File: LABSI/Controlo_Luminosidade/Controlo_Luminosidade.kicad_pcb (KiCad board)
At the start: 2 copper layers, 60 x 80 mm, 41 parts, among them J1 5V/4A, J10 Touch Button, J11 Touch Button, J12 Touch Button, J2 Barrel_Jack_Switch, J3 Conn_01x05_Pin, J4 Conn_01x04_Pin, J5 Conn_01x04_Pin, J6 AVR-ISP-6, J7 Conn_01x03_Pin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

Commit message: pcb finalizado, gee«rbers gerados, falta desenvolver o que falta no ultimo commit
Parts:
- removed C9: 0.1u, Capacitor_THT:C_Disc_D3.0mm_W2.0mm_P2.50mm
- added J13: ESP32, Connector_PinSocket_2.54mm:PinSocket_1x04_P2.54mm_Vertical, F.Cu at (135.8, 68.2)
- added R8: 6.8k, Resistor_THT:R_Axial_DIN0204_L3.6mm_D1.6mm_P5.08mm_Horizontal, F.Cu at (145.3, 71.3)
- added R9: 10k, Resistor_THT:R_Axial_DIN0204_L3.6mm_D1.6mm_P5.08mm_Horizontal, F.Cu at (140.3, 75.0)
- added REF**: MountingHole_2.2mm_M2, MountingHole:MountingHole_2.2mm_M2, F.Cu at (164.7, 61.2)
- added REF**: MountingHole_2.2mm_M2, MountingHole:MountingHole_2.2mm_M2, F.Cu at (181.6, 126.5)
- added REF**: MountingHole_2.2mm_M2, MountingHole:MountingHole_2.2mm_M2, F.Cu at (128.7, 126.5)
- J1: value 5V/4A -> Barrel_Jack_Switch
- J3, J9: value Conn_01x05_Pin -> BH1750
- J4, J5: value Conn_01x04_Pin -> HC-SR04
- J7, J8: value Conn_01x03_Pin -> SG90
- U4: value I2C_4PIN -> LCD_I2C; footprint Connector_PinHeader_2.54mm:PinHeader_2x02_P2.54mm_Vertical -> Connector_PinSocket_2.54mm:PinSocket_2x02_P2.54mm_Vertical
- moved J10 35.5 mm to (168.8, 83.3), turned to 0 degrees
- moved C2 29.3 mm to (152.9, 55.7), turned to -90 degrees
- moved J3 27.9 mm to (172.1, 54.6)
- moved C7 27.7 mm to (171.8, 58.0), turned to 180 degrees
- moved C12 24.1 mm to (175.2, 117.0)
- moved C13 21.9 mm to (171.2, 119.2), turned to -90 degrees
- moved C1 21.5 mm to (146.9, 55.7), turned to -90 degrees
- moved J7 19.4 mm to (168.9, 112.0), turned to -90 degrees
- moved C3 16.9 mm to (129.2, 101.6), turned to 180 degrees
- moved C4 16.9 mm to (129.2, 96.7), turned to 180 degrees
- moved C17 14.4 mm to (130.9, 90.7), turned to 180 degrees
- moved Q1 14.2 mm to (128.7, 112.8), turned to 0 degrees
- moved R7 12.3 mm to (162.8, 72.4), turned to 90 degrees
- moved R6 11.9 mm to (167.9, 75.7), turned to 90 degrees
- moved R3 11.8 mm to (127.0, 117.2)
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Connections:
- net /PD5/GATE renamed /PB3/GATE
- U1 pad 2: /TRIG -> /RX_ATMEGA
- U1 pad 25: unconnected-(U1-PC2-Pad25) -> /TRIG
- U1 pad 26: unconnected-(U1-PC3-Pad26) -> /TRIG2
- U1 pad 3: /TRIG2 -> /TX_ATMEGA
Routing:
- net /RX_ATMEGA: track 0.00 -> 27.9 mm
- net Net-(J10-Pin_2): track 32.0 -> 10.9 mm
- net /BUZZER: track 9.70 -> 26.0 mm
- net /PD7/SW2: track 27.1 -> 12.8 mm
- net /PD4/SW1: track 52.0 -> 37.7 mm
- net /MISO: track 9.48 -> 23.3 mm
- net /XTAL2: track 10.6 -> 24.3 mm
- net /XTAL1: track 11.2 -> 23.3 mm
- net /RX_ESP-32: track 0.00 -> 12.1 mm
- net /SERVO1: track 19.6 -> 7.65 mm
- net /SERVO2: track 17.5 -> 5.64 mm
- net /TX_ATMEGA: track 0.00 -> 9.61 mm
- net +5V: track 328.1 -> 319.0 mm
- net Net-(D1-A): track 14.3 -> 6.24 mm
- net /ECHO2: track 27.3 -> 21.4 mm
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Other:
- copper layers 2 -> 4
- board text added: "5V"
- board text added: "GND"
- board text added: "MISO"
- board text added: "MOSI"
- board text added: "RST"
- board text added: "RX"
- board text added: "SCK"
- board text added: "SCL"
- board text added: "SDA"
- board text added: "SGN"
- board text added: "TX"

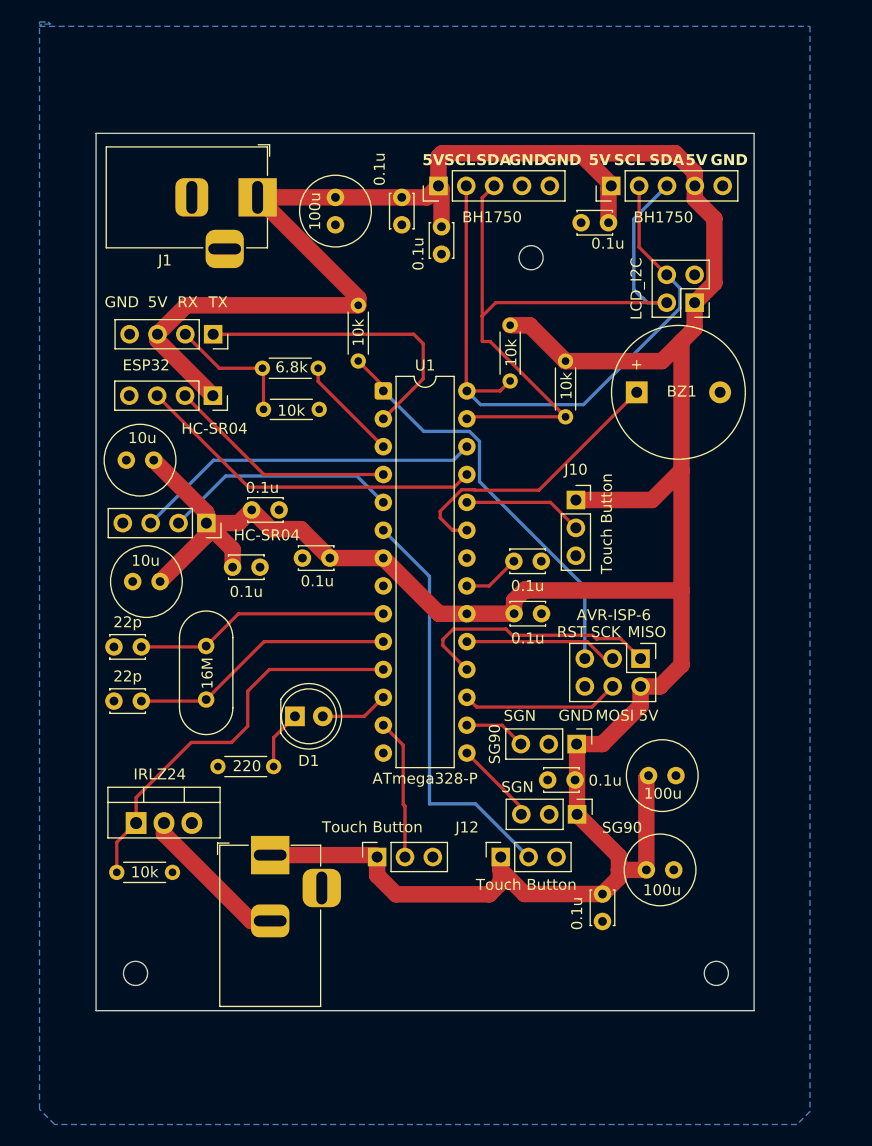
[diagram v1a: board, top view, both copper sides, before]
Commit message: pcb mudado, adicionada fusivel de 5A e Diodo tvs na entrada como proteção, gerbers gerados nao foi mexido no firmware
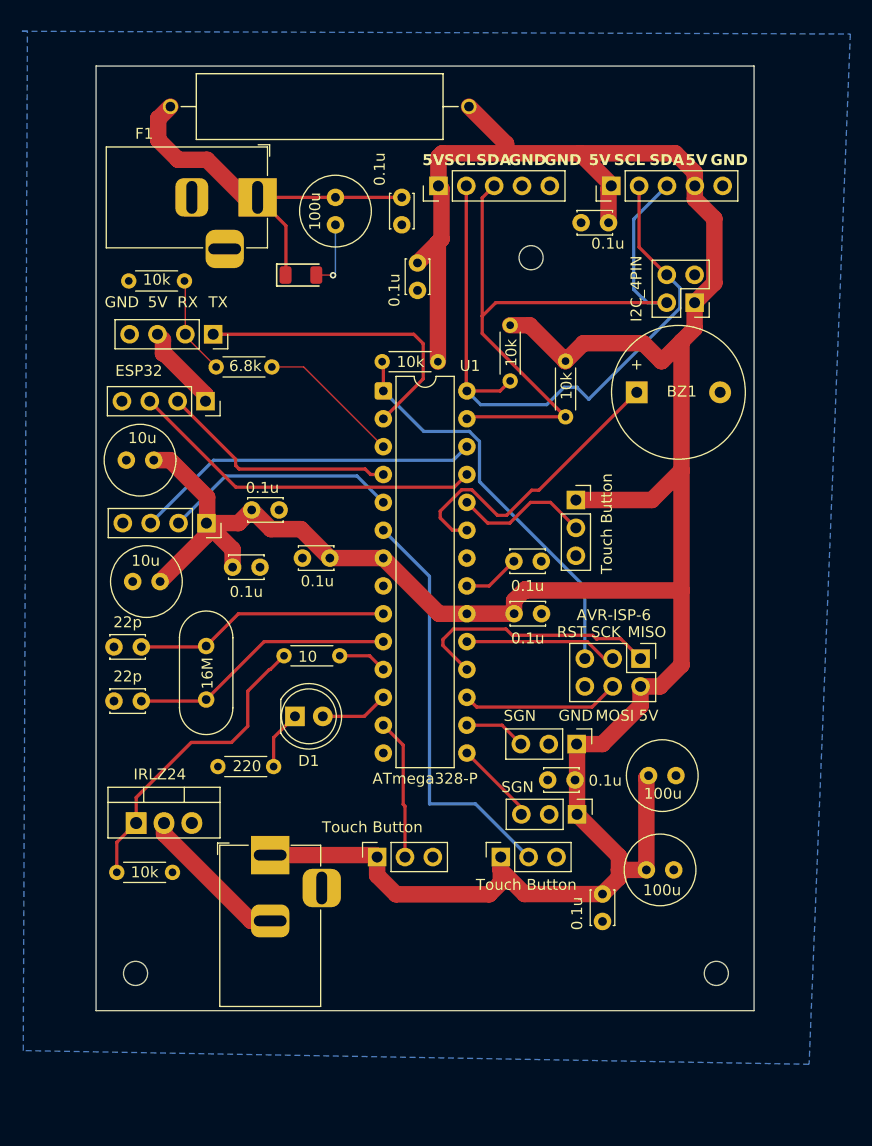
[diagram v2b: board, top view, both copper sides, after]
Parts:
- added D3: SMF7.0A, PCM_JLCPCB:D_SOD-123FL, F.Cu at (143.8, 62.8)
- added F1: Fuse, 0ADKP9160-RE:FUSAD2722W65L2250D600, F.Cu at (145.5, 47.4)
- added R10: 10, Resistor_THT:R_Axial_DIN0204_L3.6mm_D1.6mm_P5.08mm_Horizontal, F.Cu at (142.2, 97.5)
- J3, J9: value BH1750 -> Conn_01x05_Pin
- J4, J5: value HC-SR04 -> Conn_01x04_Pin
- J7, J8: value SG90 -> Conn_01x03_Pin
- U4: value LCD_I2C -> I2C_4PIN
- moved R9 13.8 mm to (133.1, 63.3), turned to 180 degrees
- moved R8 4.22 mm to (141.1, 71.2)
- moved C8 3.96 mm to (154.4, 61.7)
- moved R1 2.18 mm to (151.2, 70.7), turned to 0 degrees
- moved J5 0.84 mm to (135.1, 74.3)
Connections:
- net /RX_ATMEGA renamed /RX_ATMEGA/TX_ESP-32
- C1 pad 1: +5V -> Net-(C1-Pad1)
- C2 pad 1: +5V -> Net-(C1-Pad1)
- J1 pad 1: +5V -> Net-(C1-Pad1)
- Q1 pad 1: /PB3/GATE -> Net-(Q1-G)
- R3 pad 1: /PB3/GATE -> Net-(Q1-G)
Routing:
- net Net-(C1-Pad1): track 0.00 -> 35.8 mm
- net /PB3/GATE: track 36.8 -> 4.49 mm
- net Net-(Q1-G): track 0.00 -> 28.3 mm
- net +5V: track 319.0 -> 292.8 mm
- net GND: track 0.00 -> 6.23 mm, vias 0 -> 1
- net /TX_ATMEGA: track 9.61 -> 13.2 mm
- net /RX_ESP-32: track 12.1 -> 9.04 mm
- net /BUZZER: track 26.0 -> 27.9 mm
- net Net-(J10-Pin_2): track 10.9 -> 12.5 mm
- net /RST-AVR: track 38.1 -> 37.2 mm
- net /SCL: track 59.6 -> 60.5 mm
- net /ECHO: track 21.1 -> 21.9 mm
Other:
- board size 60 x 80 mm -> 60 x 86.1 mm
- copper layers 4 -> 2
- board text added: "PROJETO - LABSI Controlo de Luminosidade Rafael Afonso 2025/2026"

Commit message: pcb impresso. falta desenvolver codigo temporizaçao para os motores, trocar codigo display para oled i2c
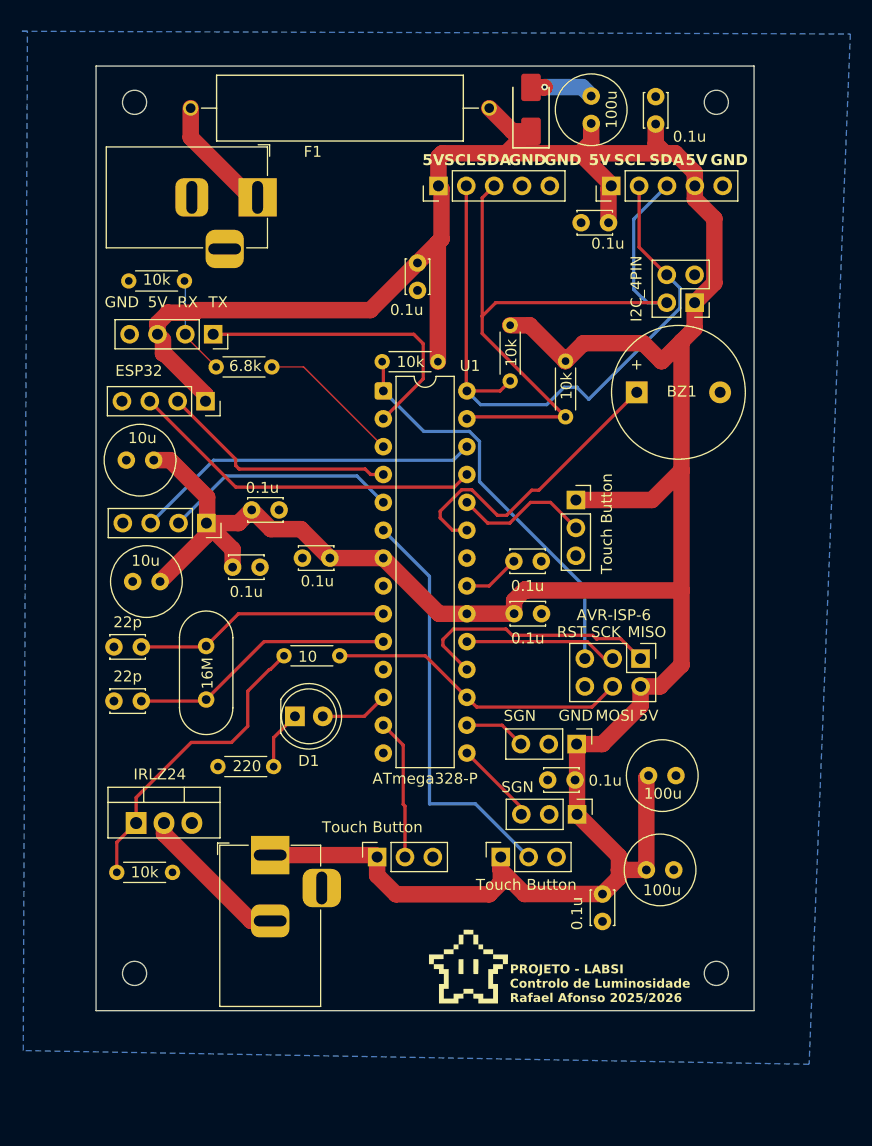
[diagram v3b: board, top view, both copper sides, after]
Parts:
- added G***: LOGO, imagens:image1, F.Cu at (159.0, 125.8)
- added REF**: MountingHole_2.2mm_M2, MountingHole:MountingHole_2.2mm_M2, F.Cu at (128.6, 47.0)
- D3: footprint PCM_JLCPCB:D_SOD-123FL -> PCM_JLCPCB:D_SMA
- moved D3 25.9 mm to (164.7, 47.7), turned to 90 degrees
- moved C1 24.3 mm to (170.2, 49.0), turned to 90 degrees
- moved C2 24.1 mm to (176.1, 49.0), turned to 90 degrees
- moved REF** 22.0 mm to (181.6, 47.0)
- moved F1 1.86 mm to (147.3, 47.6)
- moved REF** 0.09 mm to (128.6, 126.5)
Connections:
- C1 pad 1: Net-(C1-Pad1) -> +5V
- C2 pad 1: Net-(C1-Pad1) -> +5V
- D3 pad 1: Net-(C1-Pad1) -> +5V
- F1 pad 1: Net-(C1-Pad1) -> Net-(F1-Pad1)
- J1 pad 1: Net-(C1-Pad1) -> Net-(F1-Pad1)
- R10 pad 2: /PB3/GATE -> /MOSI
- U1 pad 11: /PB3/GATE -> unconnected-(U1-PD5-Pad11)
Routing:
- net Net-(C1-Pad1): track 35.8 -> 0.00 mm
- net +5V: track 292.8 -> 328.1 mm
- net /MOSI: track 14.4 -> 27.6 mm
- net Net-(F1-Pad1): track 0.00 -> 11.4 mm
- net /PB3/GATE: track 4.49 -> 0.00 mm
